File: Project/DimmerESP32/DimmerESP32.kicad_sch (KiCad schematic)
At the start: 14 parts, among them J1 Conn_01x05_Male, J2 Conn_01x04_Male, Q1 BT136-600, U1 MOC3021M, U2 4N25

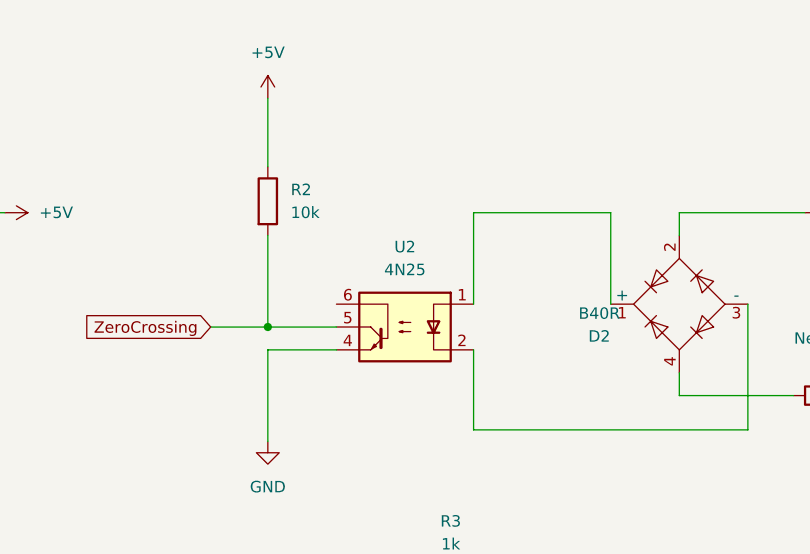
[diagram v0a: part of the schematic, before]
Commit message: Change 4N25 to TIL111
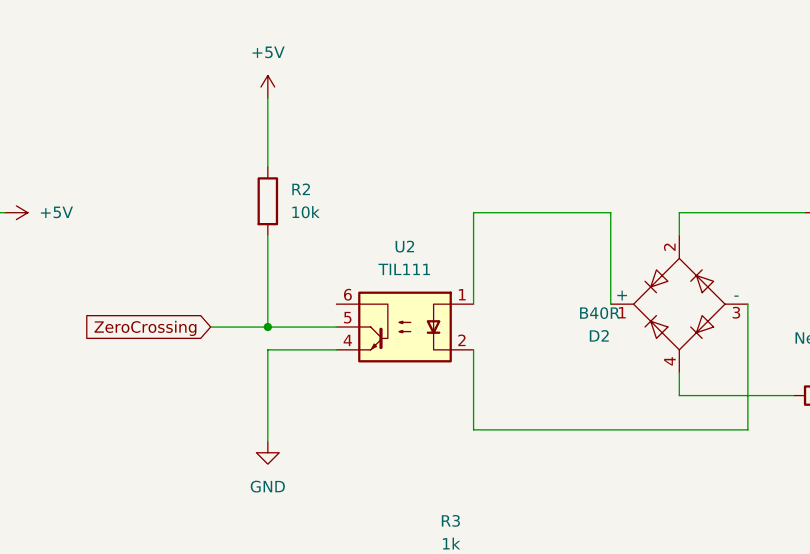
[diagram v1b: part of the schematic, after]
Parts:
- removed U2: 4N25, Package_DIP:DIP-6_W7.62mm, symbol Isolator:4N25
- added U2: TIL111, Package_DIP:DIP-6_W7.62mm, symbol Isolator:TIL111
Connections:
- net GND: now also U2.4
- net ZeroCrossing: now also U2.5
- net at D2.1 (+): now also U2.1
- net at D2.3 (-): now also U2.2
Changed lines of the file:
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@@
     (pin "1")
   )
-  (symbol (lib_id "Isolator:4N25") (at 152.4 88.9 0) (mirror y) (unit 1)
+  (symbol (lib_id "Isolator:TIL111") (at 152.4 88.9 0) (mirror y) (unit 1)
     (in_bom yes) (on_board yes) (fields_autoplaced)
     (property "Reference" "U2" (id 0) (at 152.4 80.01 0))
-    (property "Value" "4N25" (id 1) (at 152.4 82.55 0))
+    (property "Value" "TIL111" (id 1) (at 152.4 82.55 0))
     (property "Footprint" "Package_DIP:DIP-6_W7.62mm" (id 2) (at 157.48 93.98 0)
       (effects (font (size 1.27 1.27) italic) (justify left) hide)
     )
-    (property "Datasheet" "https://www.vishay.com/docs/83725/4n25.pdf" (id 3) (at 152.4 88.9 0)
+    (property "Datasheet" "https://www.egr.msu.edu/eceshop/Parts_Inventory/datasheets/til111.pdf" (id 3) (at 152.4 88.9 0)
       (effects (font (size 1.27 1.27)) (justify left) hide)
     )
@@
       (reference "U1") (unit 1) (value "MOC3021M") (footprint "Package_DIP:DIP-5-6_W7.62mm")
     )
-    (path "/4202cb78-a835-47bd-ae6b-30c40cab40be"
-      (reference "U2") (unit 1) (value "4N25") (footprint "Package_DIP:DIP-6_W7.62mm")
-    )
-  )
+    (path "/42b8ce53-a622-4824-8ad5-98283f3cc3a0"
+      (reference "U2") (unit 1) (value "TIL111") (footprint "Package_DIP:DIP-6_W7.62mm")
+    )
+  )

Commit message: Updated KiCad
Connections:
- net DimmerSignal: now also J1.4 (Pin_4); no longer J1.5 (Pin_5)
- net ZeroCrossing: no longer J2.1 (Pin_1)
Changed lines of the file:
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@@
 (kicad_sch (version 20211123) (generator eeschema)
   (paper "A4")
-  (junction (at 208.28 76.2) (diameter 0) (color 0 0 0 0)
+  (junction (at 219.71 82.55) (diameter 0) (color 0 0 0 0)
+  )
+  (junction (at 215.9 127) (diameter 0) (color 0 0 0 0)
+  )
+  (junction (at 137.16 88.9) (diameter 0) (color 0 0 0 0)
   )
   (junction (at 219.71 96.52) (diameter 0) (color 0 0 0 0)
   )
-  (junction (at 137.16 88.9) (diameter 0) (color 0 0 0 0)
-  )
-  (junction (at 217.17 85.09) (diameter 0) (color 0 0 0 0)
-  )
   (junction (at 177.8 116.84) (diameter 0) (color 0 0 0 0)
   )
-  (wire (pts (xy 217.17 85.09) (xy 217.17 127))
-    (stroke (width 0) (type default) (color 0 0 0 0))
-  )
-  (wire (pts (xy 217.17 127) (xy 224.79 127))
-    (stroke (width 0) (type default) (color 0 0 0 0))
-  )
   (wire (pts (xy 146.05 129.54) (xy 146.05 116.84))
     (stroke (width 0) (type default) (color 0 0 0 0))
@@
     (stroke (width 0) (type default) (color 0 0 0 0))
   )
+  (wire (pts (xy 215.9 127) (xy 215.9 133.35))
+    (stroke (width 0) (type default) (color 0 0 0 0))
+  )
   (wire (pts (xy 125.73 123.19) (xy 125.73 129.54))
     (stroke (width 0) (type default) (color 0 0 0 0))
@@
     (stroke (width 0) (type default) (color 0 0 0 0))
   )
+  (wire (pts (xy 69.85 77.47) (xy 74.93 77.47))
+    (stroke (width 0) (type default) (color 0 0 0 0))
+  )
   (wire (pts (xy 140.97 129.54) (xy 146.05 129.54))
     (stroke (width 0) (type default) (color 0 0 0 0))
@@
     (stroke (width 0) (type default) (color 0 0 0 0))
   )
-  (wire (pts (xy 214.63 85.09) (xy 217.17 85.09))
-    (stroke (width 0) (type default) (color 0 0 0 0))
-  )
   (wire (pts (xy 175.26 76.2) (xy 175.26 86.36))
     (stroke (width 0) (type default) (color 0 0 0 0))
   )
-  (wire (pts (xy 204.47 76.2) (xy 208.28 76.2))
+  (wire (pts (xy 215.9 127) (xy 224.79 127))
+    (stroke (width 0) (type default) (color 0 0 0 0))
+  )
+  (wire (pts (xy 215.9 85.09) (xy 215.9 127))
+    (stroke (width 0) (type default) (color 0 0 0 0))
+  )
+  (wire (pts (xy 204.47 76.2) (xy 219.71 76.2))
     (stroke (width 0) (type default) (color 0 0 0 0))
   )
@@
     (stroke (width 0) (type default) (color 0 0 0 0))
   )
-  (wire (pts (xy 177.8 116.84) (xy 208.28 116.84))
+  (wire (pts (xy 177.8 116.84) (xy 210.82 116.84))
     (stroke (width 0) (type default) (color 0 0 0 0))
   )
@@
     (stroke (width 0) (type default) (color 0 0 0 0))
   )
+  (wire (pts (xy 219.71 85.09) (xy 215.9 85.09))
+    (stroke (width 0) (type default) (color 0 0 0 0))
+  )
   (wire (pts (xy 130.81 88.9) (xy 137.16 88.9))
     (stroke (width 0) (type default) (color 0 0 0 0))
   )
-  (wire (pts (xy 69.85 90.17) (xy 69.85 80.01))
-    (stroke (width 0) (type default) (color 0 0 0 0))
-  )
   (wire (pts (xy 137.16 78.74) (xy 137.16 88.9))
     (stroke (width 0) (type default) (color 0 0 0 0))
@@
     (stroke (width 0) (type default) (color 0 0 0 0))
   )
-  (wire (pts (xy 88.9 60.96) (xy 88.9 71.12))
-    (stroke (width 0) (type default) (color 0 0 0 0))
-  )
-  (wire (pts (xy 219.71 96.52) (xy 203.2 96.52))
+  (wire (pts (xy 203.2 96.52) (xy 219.71 96.52))
+    (stroke (width 0) (type default) (color 0 0 0 0))
+  )
+  (wire (pts (xy 219.71 124.46) (xy 224.79 124.46))
     (stroke (width 0) (type default) (color 0 0 0 0))
   )
@@
     (stroke (width 0) (type default) (color 0 0 0 0))
   )
-  (wire (pts (xy 208.28 76.2) (xy 219.71 76.2))
+  (wire (pts (xy 210.82 82.55) (xy 219.71 82.55))
     (stroke (width 0) (type default) (color 0 0 0 0))
   )
@@
     (stroke (width 0) (type default) (color 0 0 0 0))
   )
-  (wire (pts (xy 224.79 124.46) (xy 219.71 124.46))
-    (stroke (width 0) (type default) (color 0 0 0 0))
-  )
   (wire (pts (xy 116.84 123.19) (xy 125.73 123.19))
     (stroke (width 0) (type default) (color 0 0 0 0))
@@
     (stroke (width 0) (type default) (color 0 0 0 0))
   )
+  (wire (pts (xy 210.82 116.84) (xy 210.82 82.55))
+    (stroke (width 0) (type default) (color 0 0 0 0))
+  )
   (wire (pts (xy 140.97 143.51) (xy 161.29 143.51))
     (stroke (width 0) (type default) (color 0 0 0 0))
@@
     (stroke (width 0) (type default) (color 0 0 0 0))
   )
+  (wire (pts (xy 88.9 76.2) (xy 107.95 76.2))
+    (stroke (width 0) (type default) (color 0 0 0 0))
+  )
+  (wire (pts (xy 74.93 87.63) (xy 74.93 77.47))
+    (stroke (width 0) (type default) (color 0 0 0 0))
+  )
+  (wire (pts (xy 195.58 96.52) (xy 182.88 96.52))
+    (stroke (width 0) (type default) (color 0 0 0 0))
+  )
   (wire (pts (xy 219.71 96.52) (xy 219.71 124.46))
     (stroke (width 0) (type default) (color 0 0 0 0))
   )
-  (wire (pts (xy 88.9 76.2) (xy 107.95 76.2))
-    (stroke (width 0) (type default) (color 0 0 0 0))
-  )
-  (wire (pts (xy 195.58 96.52) (xy 182.88 96.52))
-    (stroke (width 0) (type default) (color 0 0 0 0))
-  )
   (wire (pts (xy 97.79 78.74) (xy 88.9 78.74))
     (stroke (width 0) (type default) (color 0 0 0 0))
@@
   )
   (wire (pts (xy 224.79 146.05) (xy 224.79 129.54))
-    (stroke (width 0) (type default) (color 0 0 0 0))
-  )
-  (wire (pts (xy 217.17 85.09) (xy 219.71 85.09))
-    (stroke (width 0) (type default) (color 0 0 0 0))
-  )
-  (wire (pts (xy 208.28 116.84) (xy 208.28 76.2))
     (stroke (width 0) (type default) (color 0 0 0 0))
   )
@@
     )
   )
-  (global_label "ZeroCrossing" (shape input) (at 88.9 60.96 0) (fields_autoplaced)
+  (global_label "ZeroCrossing" (shape input) (at 72.39 91.44 0) (fields_autoplaced)
     (effects (font (size 1.27 1.27)) (justify left))
-    (property "Intersheet References" "${INTERSHEET_REFS}" (id 0) (at 103.7107 60.8806 0)
+    (property "Intersheet References" "${INTERSHEET_REFS}" (id 0) (at 87.2007 91.3606 0)
       (effects (font (size 1.27 1.27)) (justify left) hide)
     )
@@
     )
   )
-  (global_label "DimmerSignal" (shape input) (at 69.85 90.17 0) (fields_autoplaced)
+  (global_label "DimmerSignal" (shape input) (at 74.93 87.63 0) (fields_autoplaced)
     (effects (font (size 1.27 1.27)) (justify left))
-    (property "Intersheet References" "${INTERSHEET_REFS}" (id 0) (at 85.326 90.0906 0)
+    (property "Intersheet References" "${INTERSHEET_REFS}" (id 0) (at 90.406 87.5506 0)
       (effects (font (size 1.27 1.27)) (justify left) hide)
     )
@@
     (pin "4")
     (pin "5")
-  )
-  (symbol (lib_id "power:Earth") (at 214.63 85.09 270) (unit 1)
-    (in_bom yes) (on_board yes) (fields_autoplaced)
-    (property "Reference" "#PWR05" (id 0) (at 208.28 85.09 0)
-      (effects (font (size 1.27 1.27)) hide)
-    )
-    (property "Value" "Earth" (id 1) (at 210.82 85.09 0)
-      (effects (font (size 1.27 1.27)) hide)
-    )
-    (property "Footprint" "" (id 2) (at 214.63 85.09 0)
-      (effects (font (size 1.27 1.27)) hide)
-    )
-    (property "Datasheet" "~" (id 3) (at 214.63 85.09 0)
-      (effects (font (size 1.27 1.27)) hide)
-    )
-    (pin "1")
   )
   (symbol (lib_id "Isolator:TIL111") (at 152.4 88.9 0) (mirror y) (unit 1)
@@
     (pin "1")
   )
+  (symbol (lib_id "power:Earth") (at 215.9 133.35 0) (unit 1)
+    (in_bom yes) (on_board yes) (fields_autoplaced)
+    (property "Reference" "#PWR?" (id 0) (at 215.9 139.7 0)
+      (effects (font (size 1.27 1.27)) hide)
+    )
+    (property "Value" "Earth" (id 1) (at 215.9 137.16 0)
+      (effects (font (size 1.27 1.27)) hide)
+    )
+    (property "Footprint" "" (id 2) (at 215.9 133.35 0)
+      (effects (font (size 1.27 1.27)) hide)
+    )
+    (property "Datasheet" "~" (id 3) (at 215.9 133.35 0)
+      (effects (font (size 1.27 1.27)) hide)
+    )
+    (pin "1")
+  )
   (sheet_instances
     (path "/" (page "1"))
@@
       (reference "#PWR03") (unit 1) (value "GND") (footprint "")
     )
-    (path "/3f2263d4-55e6-44cc-aef3-cfa7733cb366"
-      (reference "#PWR05") (unit 1) (value "Earth") (footprint "")
-    )
     (path "/69dce165-0a76-4e51-a7c5-2a1fe5e35283"
       (reference "#PWR0101") (unit 1) (value "+3V3") (footprint "")
@@
       (reference "#PWR0103") (unit 1) (value "GND") (footprint "")
     )
+    (path "/d4f96528-cd2a-48fd-b567-62e5b218cda7"
+      (reference "#PWR?") (unit 1) (value "Earth") (footprint "")
+    )
     (path "/873928c0-bd88-4dd1-b711-8ae9ae3b7feb"

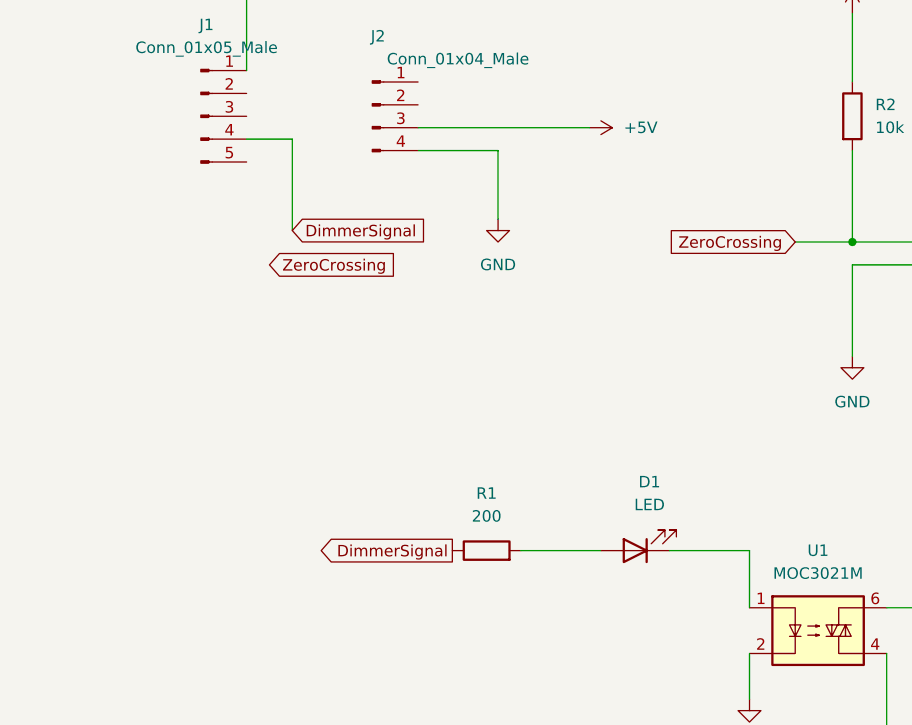
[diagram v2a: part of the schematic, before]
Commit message: Remove LED and resistor from schem and PCB
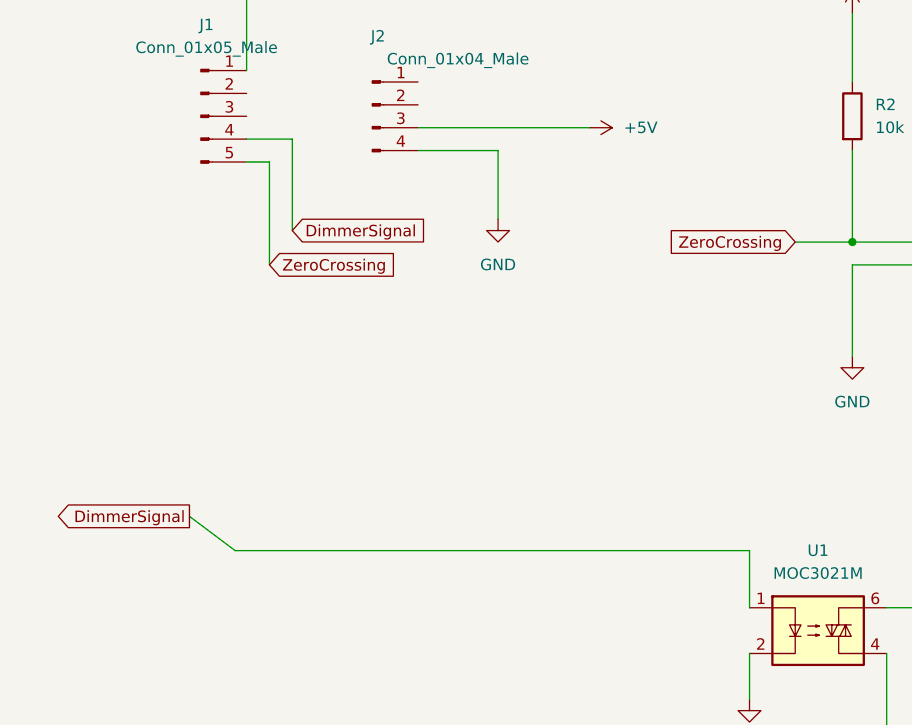
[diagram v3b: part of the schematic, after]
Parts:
- removed D1: LED, LED_THT:LED_D3.0mm, symbol Device:LED
- removed R1: 200, Resistor_THT:R_Axial_DIN0207_L6.3mm_D2.5mm_P10.16mm_Horizontal, symbol Device:R
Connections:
- net DimmerSignal: now also U1.1
- net ZeroCrossing: now also J1.5 (Pin_5)
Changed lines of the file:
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@@
+    (stroke (width 0) (type default) (color 0 0 0 0))
+  )
+  (wire (pts (xy 69.85 80.01) (xy 72.39 80.01))
     (stroke (width 0) (type default) (color 0 0 0 0))
   )
@@
     (stroke (width 0) (type default) (color 0 0 0 0))
   )
+  (wire (pts (xy 68.58 123.19) (xy 63.5 119.38))
+    (stroke (width 0) (type default) (color 0 0 0 0))
+  )
   (wire (pts (xy 219.71 124.46) (xy 224.79 124.46))
     (stroke (width 0) (type default) (color 0 0 0 0))
@@
     (stroke (width 0) (type default) (color 0 0 0 0))
   )
-  (wire (pts (xy 116.84 123.19) (xy 125.73 123.19))
+  (wire (pts (xy 68.58 123.19) (xy 125.73 123.19))
     (stroke (width 0) (type default) (color 0 0 0 0))
   )
@@
     (stroke (width 0) (type default) (color 0 0 0 0))
   )
-  (wire (pts (xy 100.33 123.19) (xy 109.22 123.19))
-    (stroke (width 0) (type default) (color 0 0 0 0))
-  )
   (wire (pts (xy 182.88 96.52) (xy 182.88 93.98))
+    (stroke (width 0) (type default) (color 0 0 0 0))
+  )
+  (wire (pts (xy 72.39 80.01) (xy 72.39 91.44))
     (stroke (width 0) (type default) (color 0 0 0 0))
   )
@@
     )
   )
-  (global_label "DimmerSignal" (shape output) (at 92.71 123.19 180) (fields_autoplaced)
+  (global_label "DimmerSignal" (shape output) (at 63.5 119.38 180) (fields_autoplaced)
     (effects (font (size 1.27 1.27)) (justify right))
-    (property "Intersheet References" "${INTERSHEET_REFS}" (id 0) (at 77.234 123.1106 0)
+    (property "Intersheet References" "${INTERSHEET_REFS}" (id 0) (at 48.024 119.3006 0)
       (effects (font (size 1.27 1.27)) (justify right) hide)
     )
@@
     (pin "3")
   )
-  (symbol (lib_id "Device:R") (at 96.52 123.19 90) (unit 1)
-    (in_bom yes) (on_board yes) (fields_autoplaced)
-    (property "Reference" "R1" (id 0) (at 96.52 116.84 90))
-    (property "Value" "200" (id 1) (at 96.52 119.38 90))
-    (property "Footprint" "Resistor_THT:R_Axial_DIN0207_L6.3mm_D2.5mm_P10.16mm_Horizontal" (id 2) (at 96.52 124.968 90)
-      (effects (font (size 1.27 1.27)) hide)
-    )
-    (property "Datasheet" "~" (id 3) (at 96.52 123.19 0)
-      (effects (font (size 1.27 1.27)) hide)
-    )
-    (pin "1")
-    (pin "2")
-  )
   (symbol (lib_id "power:+3V3") (at 69.85 60.96 0) (unit 1)
     (in_bom yes) (on_board yes) (fields_autoplaced)
@@
     )
     (pin "1")
-  )
-  (symbol (lib_id "Device:LED") (at 113.03 123.19 180) (unit 1)
-    (in_bom yes) (on_board yes) (fields_autoplaced)
-    (property "Reference" "D1" (id 0) (at 114.6175 115.57 0))
-    (property "Value" "LED" (id 1) (at 114.6175 118.11 0))
-    (property "Footprint" "LED_THT:LED_D3.0mm" (id 2) (at 113.03 123.19 0)
-      (effects (font (size 1.27 1.27)) hide)
-    )
-    (property "Datasheet" "~" (id 3) (at 113.03 123.19 0)
-      (effects (font (size 1.27 1.27)) hide)
-    )
-    (pin "1")
-    (pin "2")
   )
   (symbol (lib_id "Device:R") (at 200.66 76.2 90) (unit 1)
@@
       (reference "#PWR?") (unit 1) (value "Earth") (footprint "")
     )
-    (path "/873928c0-bd88-4dd1-b711-8ae9ae3b7feb"
-      (reference "D1") (unit 1) (value "LED") (footprint "LED_THT:LED_D3.0mm")
-    )
     (path "/5641be26-f5e9-482f-8616-297f17f4eae2"
       (reference "D2") (unit 1) (value "B40R") (footprint "Diode_THT:Diode_Bridge_Round_D9.0mm")
@@
       (reference "Q1") (unit 1) (value "BT136-600") (footprint "Package_TO_SOT_THT:TO-220-3_Vertical")
     )
-    (path "/6642fc52-a8a5-46d7-baa8-3fa36d7485f9"
-      (reference "R1") (unit 1) (value "200") (footprint "Resistor_THT:R_Axial_DIN0207_L6.3mm_D2.5mm_P10.16mm_Horizontal")
-    )
     (path "/c99a01e4-5eaa-46e4-a099-2595cfae2e64"
